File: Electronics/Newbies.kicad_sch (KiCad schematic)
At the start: 40 parts, among them J1 USB_C_Receptacle_USB2.0_14P, J2 Screw_Terminal_01x04, J3 Screw_Terminal_01x04, SW1 SW_Push, SW2 SW_Push, SW3 SW_Push, SW4 SW_Push, SW5 SW_Push, SW6 SW_Push, U1 ESP32-S3-WROOM-1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

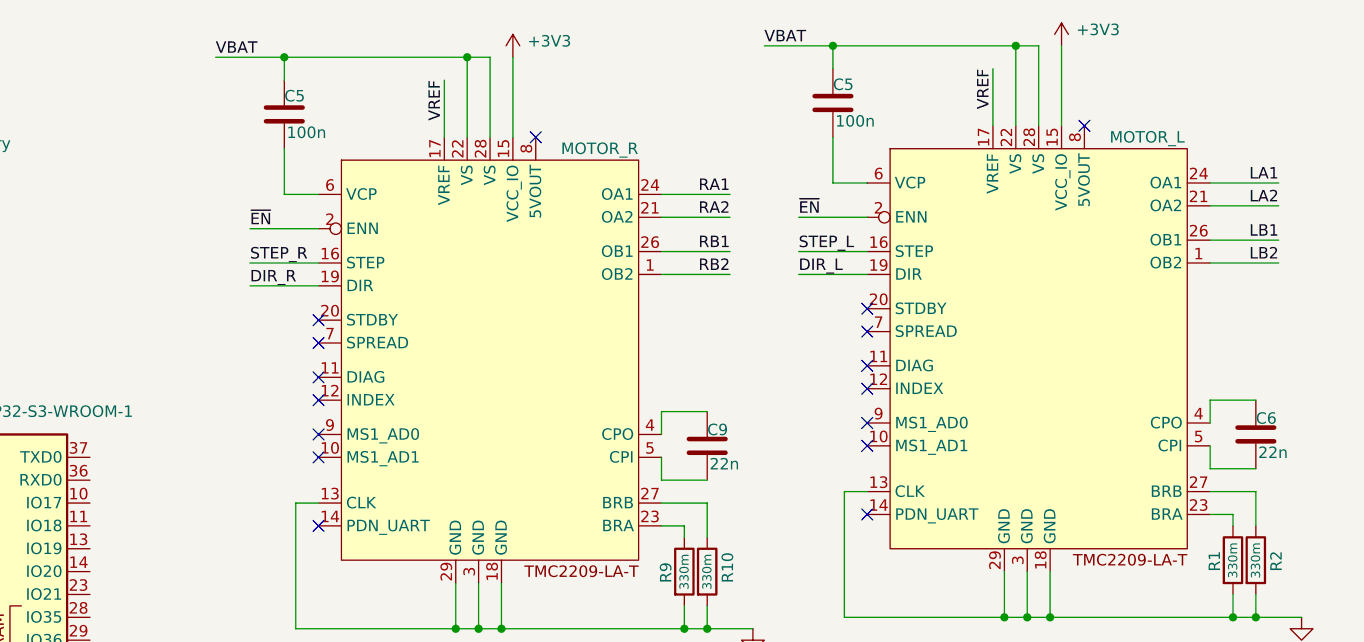
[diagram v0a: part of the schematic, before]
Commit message: Set spread SpreadCycle
Tied the Spread pins to high, for better positional accuracy www.klipper3d.org/TMC_Drivers.html
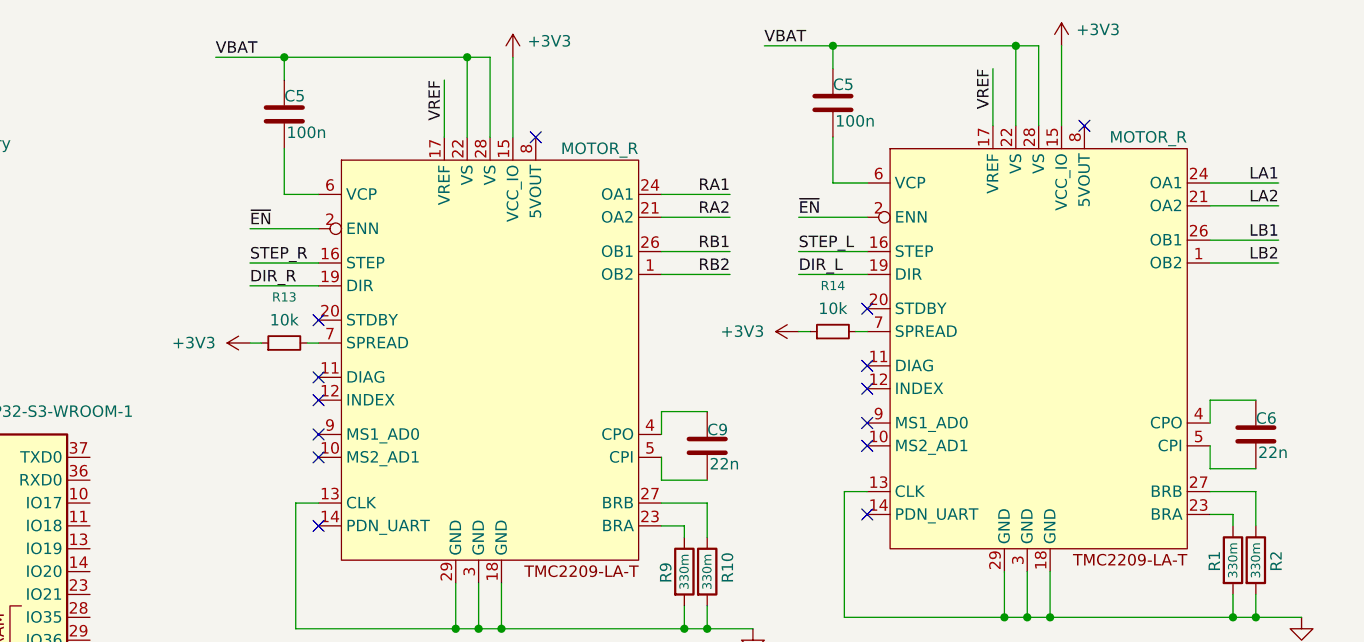
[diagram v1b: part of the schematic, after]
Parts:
- added R13, R14: 10k, symbol Device:R_Small
- U4: value MOTOR_L -> MOTOR_R
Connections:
- net +3V3: now also R13.1, R14.1
- net at U4.7 (SPREAD): now also R14.2
- net at U4.7 (SPREAD): now also R13.2
- no-connect marks 18 -> 16

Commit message: Finish wiring up the DAC
SCL & SDA wires. And I think vout is for tmc vref.
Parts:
- added C11: 0.1u, symbol Device:C
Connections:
- net +3V3: now also U6.6 (VA), U6.7 (VREF), C11.1
- net GND: now also C11.2
- net SCL: now also U6.3 (SCL)
- net SDA: now also U6.4 (SDA)
- net VREF: now also U6.8 (VOUT)
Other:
- moved on the sheet: C10, R11, R12, SW1, SW2, U6

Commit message: 1/32 Microstepping
Connected MS1 to 3v3
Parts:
- removed R13, R14: 10k, symbol Device:R_Small
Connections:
- net +3V3: now also U4.7 (SPREAD), U4.7 (SPREAD), U4.9 (MS1_AD0), U4.9 (MS1_AD0)
- no-connect marks 16 -> 14
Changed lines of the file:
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@@
 	)
 	(no_connect
-		(at 144.78 62.23)
-	)
-	(no_connect
 		(at 144.78 58.42)
 	)
 	(no_connect
-		(at 205.74 60.96)
-	)
-	(no_connect
 		(at 144.78 72.39)
 	)
@@
 	(wire
 		(pts
+			(xy 203.2 60.96) (xy 205.74 60.96)
+		)
+		(stroke
+			(width 0)
+			(type default)
+		)
+	)
+	(wire
+		(pts
 			(xy 78.74 100.33) (xy 88.9 100.33)
 		)
@@
 	(wire
 		(pts
+			(xy 142.24 62.23) (xy 144.78 62.23)
+		)
+		(stroke
+			(width 0)
+			(type default)
+		)
+	)
+	(wire
+		(pts
 			(xy 171.45 111.76) (xy 171.45 109.22)
 		)
@@
 	(wire
 		(pts
-			(xy 204.47 50.8) (xy 205.74 50.8)
-		)
-		(stroke
-			(width 0)
-			(type default)
-		)
-	)
-	(wire
-		(pts
 			(xy 78.74 105.41) (xy 88.9 105.41)
 		)
@@
 	(wire
 		(pts
-			(xy 198.12 50.8) (xy 199.39 50.8)
+			(xy 204.47 50.8) (xy 205.74 50.8)
 		)
 		(stroke
@@
 	(wire
 		(pts
-			(xy 143.51 52.07) (xy 144.78 52.07)
-		)
-		(stroke
-			(width 0)
-			(type default)
-		)
-	)
-	(wire
-		(pts
 			(xy 60.96 146.05) (xy 67.31 146.05)
 		)
@@
 	(wire
 		(pts
-			(xy 137.16 52.07) (xy 138.43 52.07)
+			(xy 143.51 52.07) (xy 144.78 52.07)
 		)
 		(stroke
@@
 	)
 	(symbol
-		(lib_id "Device:R_Small")
-		(at 140.97 52.07 90)
-		(unit 1)
-		(exclude_from_sim no)
-		(in_bom yes)
-		(on_board yes)
-		(dnp no)
-		(fields_autoplaced yes)
-		(property "Reference" "R13"
-			(at 140.97 46.99 90)
-			(effects
-				(font
-					(size 1.016 1.016)
-				)
-			)
-		)
-		(property "Value" "10k"
-			(at 140.97 49.53 90)
-			(effects
-				(font
-					(size 1.27 1.27)
-				)
-			)
-		)
-		(property "Footprint" ""
-			(at 140.97 52.07 0)
-			(effects
-				(font
-					(size 1.27 1.27)
-				)
-				(hide yes)
-			)
-		)
-		(property "Datasheet" "~"
-			(at 140.97 52.07 0)
-			(effects
-				(font
-					(size 1.27 1.27)
-				)
-				(hide yes)
-			)
-		)
-		(property "Description" "Resistor, small symbol"
-			(at 140.97 52.07 0)
-			(effects
-				(font
-					(size 1.27 1.27)
-				)
-				(hide yes)
-			)
-		)
-		(pin "1"
-		)
-		(pin "2"
-		)
-		(instances
-			(project ""
-				(path "/fd18eede-8399-4127-a462-c13ac3c83e77"
-					(reference "R13")
-					(unit 1)
-				)
-			)
-		)
-	)
-	(symbol
 		(lib_id "RF_Module:ESP32-S3-WROOM-1")
 		(at 104.14 87.63 0)
@@
 	)
 	(symbol
-		(lib_id "Device:R_Small")
-		(at 201.93 50.8 90)
-		(unit 1)
-		(exclude_from_sim no)
-		(in_bom yes)
-		(on_board yes)
-		(dnp no)
-		(fields_autoplaced yes)
-		(property "Reference" "R14"
-			(at 201.93 45.72 90)
-			(effects
-				(font
-					(size 1.016 1.016)
-				)
-			)
-		)
-		(property "Value" "10k"
-			(at 201.93 48.26 90)
-			(effects
-				(font
-					(size 1.27 1.27)
-				)
-			)
-		)
-		(property "Footprint" ""
-			(at 201.93 50.8 0)
-			(effects
-				(font
-					(size 1.27 1.27)
-				)
-				(hide yes)
-			)
-		)
-		(property "Datasheet" "~"
-			(at 201.93 50.8 0)
-			(effects
-				(font
-					(size 1.27 1.27)
-				)
-				(hide yes)
-			)
-		)
-		(property "Description" "Resistor, small symbol"
-			(at 201.93 50.8 0)
-			(effects
-				(font
-					(size 1.27 1.27)
-				)
-				(hide yes)
-			)
-		)
-		(pin "1"
-		)
-		(pin "2"
-		)
-		(instances
-			(project ""
-				(path "/fd18eede-8399-4127-a462-c13ac3c83e77"
-					(reference "R14")
-					(unit 1)
-				)
-			)
-		)
-	)
-	(symbol
 		(lib_id "Device:R")
 		(at 180.34 115.57 90)
@@
 		(lib_name "+3V3_4")
 		(lib_id "power:+3V3")
-		(at 198.12 50.8 90)
+		(at 204.47 50.8 90)
 		(unit 1)
 		(exclude_from_sim no)
@@
 		(fields_autoplaced yes)
 		(property "Reference" "#PWR029"
-			(at 201.93 50.8 0)
+			(at 208.28 50.8 0)
 			(effects
 				(font
@@
 		)
 		(property "Value" "+3V3"
-			(at 194.31 50.7999 90)
+			(at 200.66 50.7999 90)
 			(effects
 				(font
@@
 		)
 		(property "Footprint" ""
-			(at 198.12 50.8 0)
+			(at 204.47 50.8 0)
 			(effects
 				(font
@@
 		)
 		(property "Datasheet" ""
-			(at 198.12 50.8 0)
+			(at 204.47 50.8 0)
 			(effects
 				(font
@@
 		)
 		(property "Description" "Power symbol creates a global label with name \"+3V3\""
-			(at 198.12 50.8 0)
+			(at 204.47 50.8 0)
 			(effects
 				(font
@@
 	)
 	(symbol
+		(lib_name "+3V3_7")
+		(lib_id "power:+3V3")
+		(at 203.2 60.96 90)
+		(unit 1)
+		(exclude_from_sim no)
+		(in_bom yes)
+		(on_board yes)
+		(dnp no)
+		(fields_autoplaced yes)
+		(property "Reference" "#PWR032"
+			(at 207.01 60.96 0)
+			(effects
+				(font
+					(size 1.27 1.27)
+				)
+				(hide yes)
+			)
+		)
+		(property "Value" "+3V3"
+			(at 199.39 60.9599 90)
+			(effects
+				(font
+					(size 1.27 1.27)
+				)
+				(justify left)
+			)
+		)
+		(property "Footprint" ""
+			(at 203.2 60.96 0)
+			(effects
+				(font
+					(size 1.27 1.27)
+				)
+				(hide yes)
+			)
+		)
+		(property "Datasheet" ""
+			(at 203.2 60.96 0)
+			(effects
+				(font
+					(size 1.27 1.27)
+				)
+				(hide yes)
+			)
+		)
+		(property "Description" "Power symbol creates a global label with name \"+3V3\""
+			(at 203.2 60.96 0)
+			(effects
+				(font
+					(size 1.27 1.27)
+				)
+				(hide yes)
+			)
+		)
+		(pin "1"
+		)
+		(instances
+			(project ""
+				(path "/fd18eede-8399-4127-a462-c13ac3c83e77"
+					(reference "#PWR032")
+					(unit 1)
+				)
+			)
+		)
+	)
+	(symbol
 		(lib_id "Device:C")
 		(at 158.75 185.42 270)
@@
 	)
 	(symbol
+		(lib_name "+3V3_6")
+		(lib_id "power:+3V3")
+		(at 142.24 62.23 90)
+		(unit 1)
+		(exclude_from_sim no)
+		(in_bom yes)
+		(on_board yes)
+		(dnp no)
+		(fields_autoplaced yes)
+		(property "Reference" "#PWR031"
+			(at 146.05 62.23 0)
+			(effects
+				(font
+					(size 1.27 1.27)
+				)
+				(hide yes)
+			)
+		)
+		(property "Value" "+3V3"
+			(at 138.43 62.2299 90)
+			(effects
+				(font
+					(size 1.27 1.27)
+				)
+				(justify left)
+			)
+		)
+		(property "Footprint" ""
+			(at 142.24 62.23 0)
+			(effects
+				(font
+					(size 1.27 1.27)
+				)
+				(hide yes)
+			)
+		)
+		(property "Datasheet" ""
+			(at 142.24 62.23 0)
+			(effects
+				(font
+					(size 1.27 1.27)
+				)
+				(hide yes)
+			)
+		)
+		(property "Description" "Power symbol creates a global label with name \"+3V3\""
+			(at 142.24 62.23 0)
+			(effects
+				(font
+					(size 1.27 1.27)
+				)
+				(hide yes)
+			)
+		)
+		(pin "1"
+		)
+		(instances
+			(project ""
+				(path "/fd18eede-8399-4127-a462-c13ac3c83e77"
+					(reference "#PWR031")
+					(unit 1)
+				)
+			)
+		)
+	)
+	(symbol
 		(lib_id "Device:C")
 		(at 57.15 34.29 0)
@@
 		(lib_name "+3V3_3")
 		(lib_id "power:+3V3")
-		(at 137.16 52.07 90)
+		(at 143.51 52.07 90)
 		(unit 1)
 		(exclude_from_sim no)
@@
 		(dnp no)
 		(property "Reference" "#PWR028"
-			(at 140.97 52.07 0)
+			(at 147.32 52.07 0)
 			(effects
 				(font
@@
 		)
 		(property "Value" "+3V3"
-			(at 133.35 52.0699 90)
+			(at 139.7 52.0699 90)
 			(effects
 				(font
@@
 		)
 		(property "Footprint" ""
-			(at 137.16 52.07 0)
+			(at 143.51 52.07 0)
 			(effects
 				(font
@@
 		)
 		(property "Datasheet" ""
-			(at 137.16 52.07 0)
+			(at 143.51 52.07 0)
 			(effects
 				(font
@@
 		)
 		(property "Description" "Power symbol creates a global label with name \"+3V3\""
-			(at 137.16 52.07 0)
+			(at 143.51 52.07 0)
 			(effects
 				(font

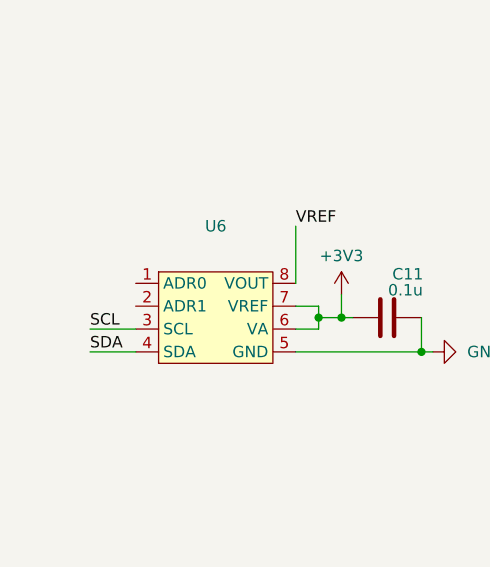
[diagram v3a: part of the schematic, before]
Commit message: Set DAC address to 0xD (Pulled ADR0 to GND)
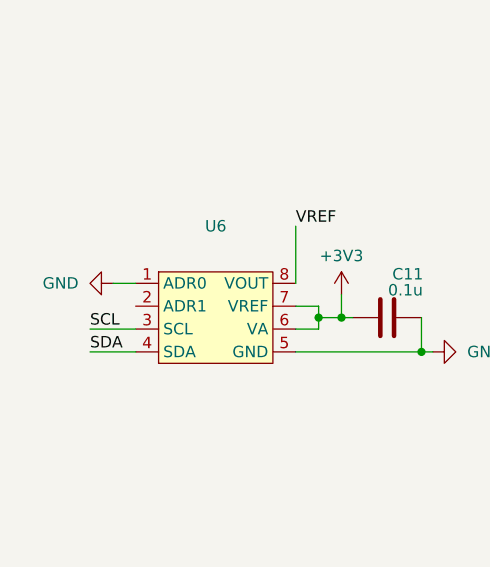
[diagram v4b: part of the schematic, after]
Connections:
- net GND: now also U6.1 (ADR0)
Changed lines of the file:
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@@
+	(wire
+		(pts
+			(xy 26.67 74.93) (xy 29.21 74.93)
+		)
+		(stroke
+			(width 0)
+			(type default)
+		)
+	)
 	(wire
 		(pts
@@
 					(unit 1)
 				)
+			)
+		)
+	)
+	(symbol
+		(lib_name "GND_5")
+		(lib_id "power:GND")
+		(at 26.67 74.93 270)
+		(unit 1)
+		(exclude_from_sim no)
+		(in_bom yes)
+		(on_board yes)
+		(dnp no)
+		(fields_autoplaced yes)
+		(property "Reference" "#PWR033"
+			(at 20.32 74.93 0)
+			(effects
+				(font
+					(size 1.27 1.27)
+				)
+				(hide yes)
+			)
+		)
+		(property "Value" "GND"
+			(at 22.86 74.9299 90)
+			(effects
+				(font
+					(size 1.27 1.27)
+				)
+				(justify right)
+			)
+		)
+		(property "Footprint" ""
+			(at 26.67 74.93 0)
+			(effects
+				(font
+					(size 1.27 1.27)
+				)
+				(hide yes)
+			)
+		)
+		(property "Datasheet" ""
+			(at 26.67 74.93 0)
+			(effects
+				(font
+					(size 1.27 1.27)
+				)
+				(hide yes)
+			)
+		)
+		(property "Description" "Power symbol creates a global label with name \"GND\" , ground"
+			(at 26.67 74.93 0)
+			(effects
+				(font
+					(size 1.27 1.27)
+				)
+				(hide yes)
+			)
+		)
+		(pin "1"
+		)
+		(instances
+			(project ""
+				(path "/fd18eede-8399-4127-a462-c13ac3c83e77"
+					(reference "#PWR033")
+					(unit 1)
+				)
